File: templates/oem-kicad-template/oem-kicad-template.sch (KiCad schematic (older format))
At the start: 25 parts

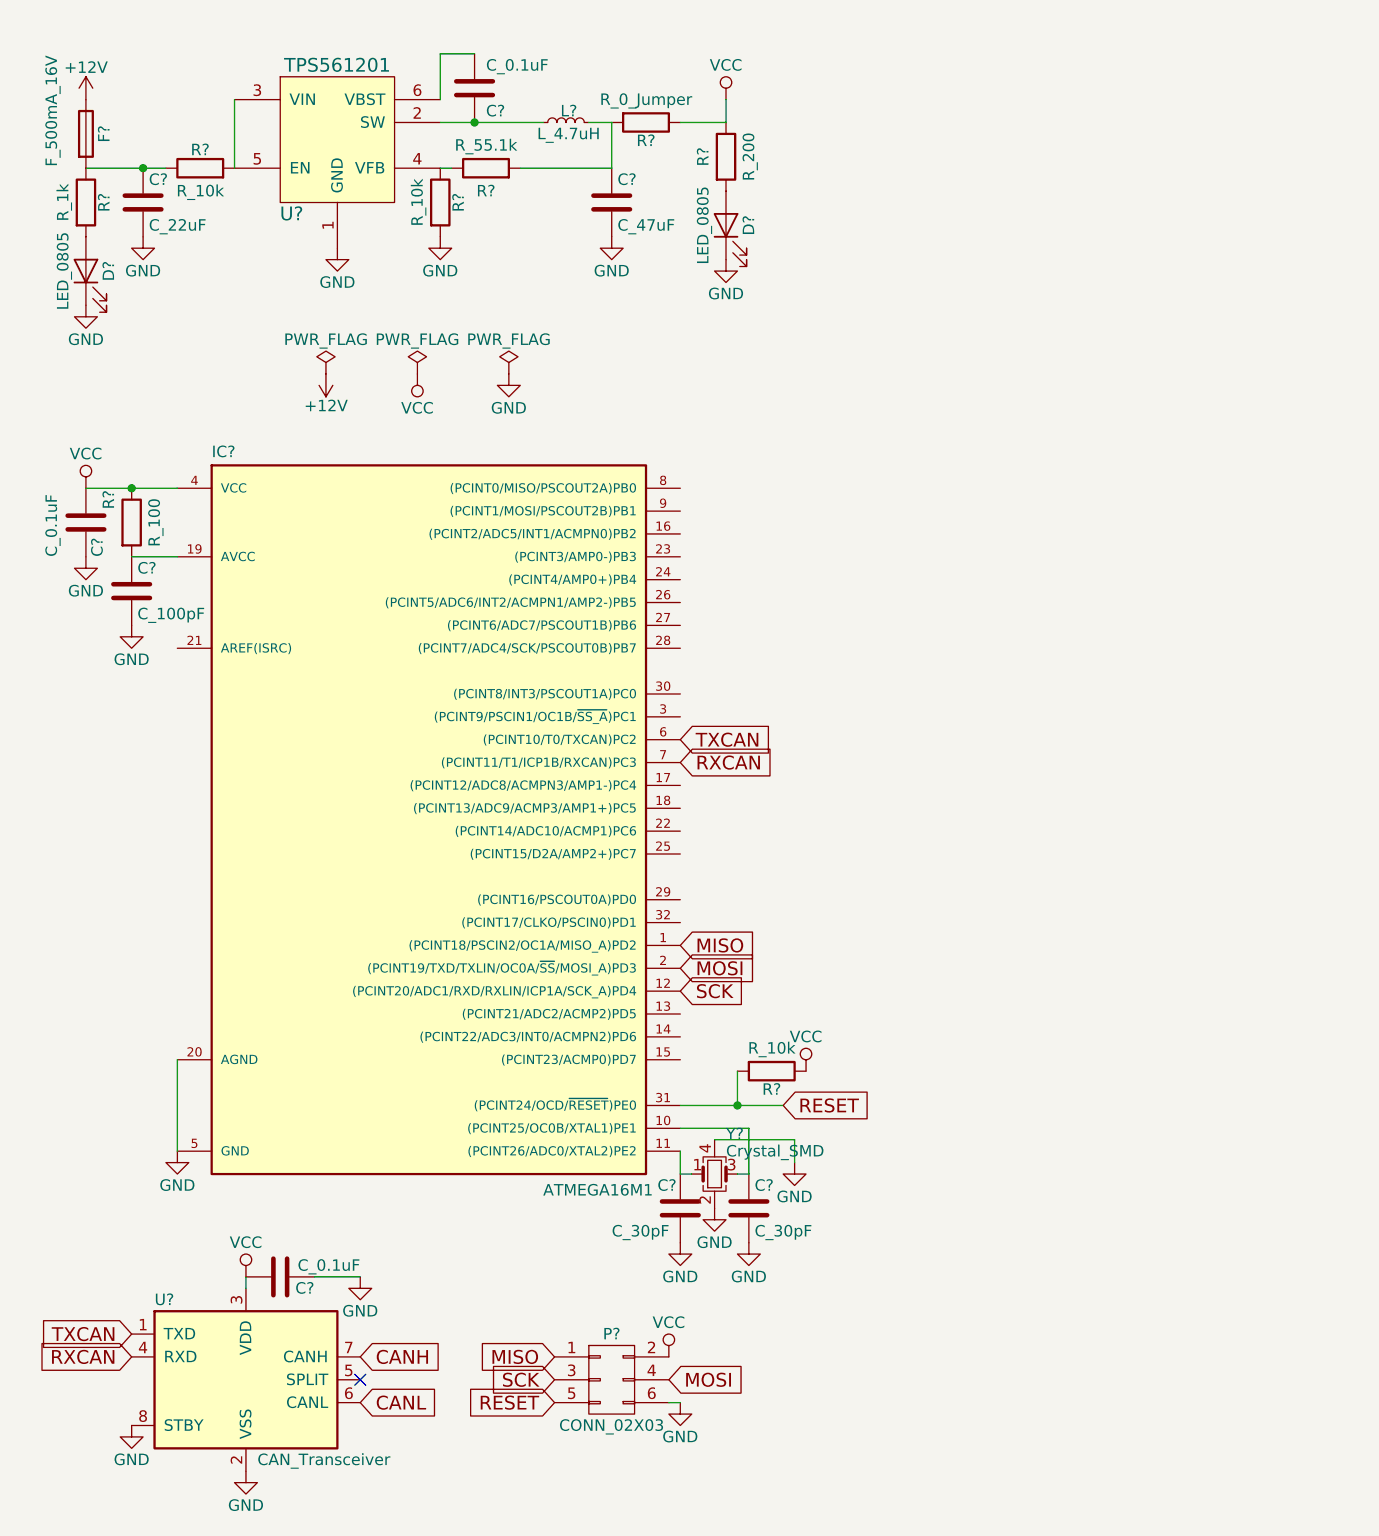
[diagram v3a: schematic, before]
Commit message: added some text to the reference schematic
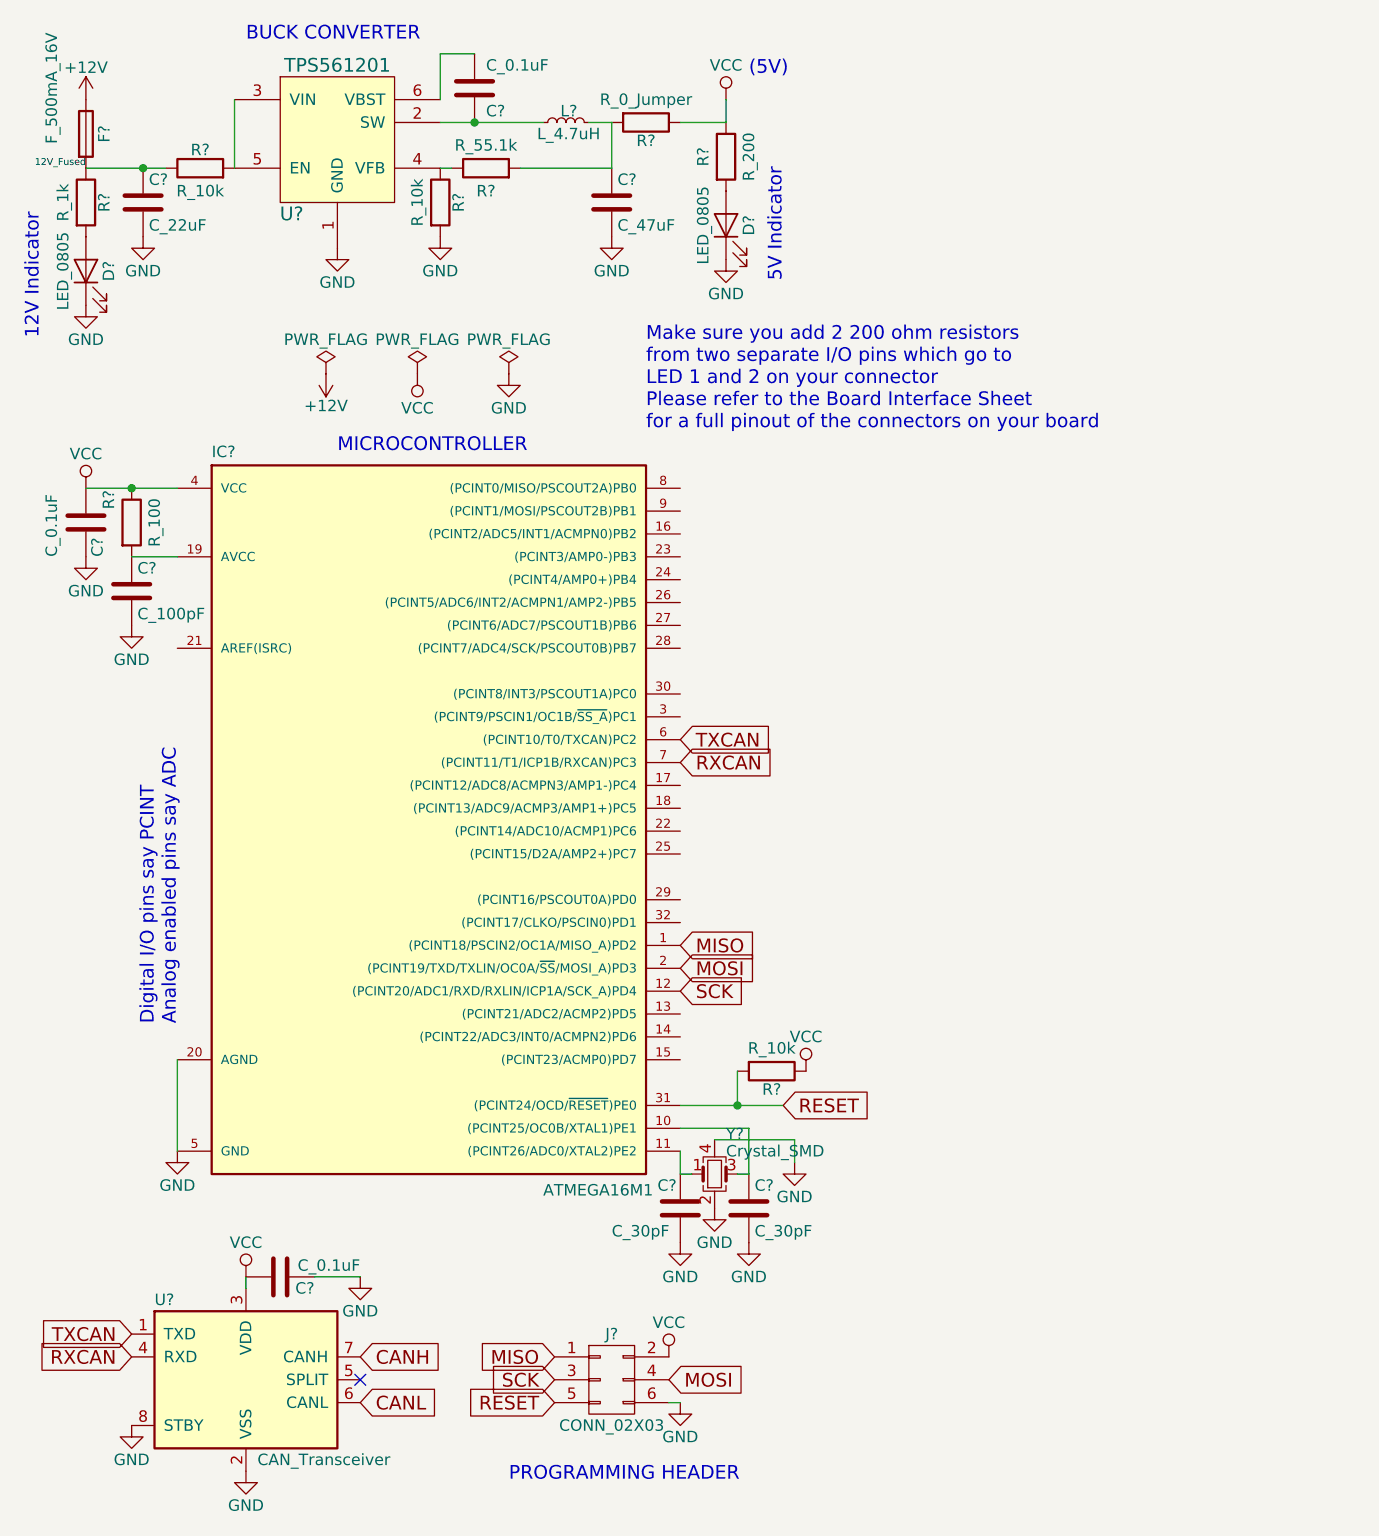
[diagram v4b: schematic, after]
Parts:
- gave numbers to parts that had none: 1
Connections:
- net 12V_Fused: now reaches C?.1, F?.2, R?.1, R?.1
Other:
- note added: "(5V)"
- note added: "12V Indicator"
- note added: "5V Indicator"
- note added: "BUCK CONVERTER"
- note added: "Digital I/O pins say PCINT\nAnalog enabled pins say ADC"
- note added: "MICROCONTROLLER"
- note added: "Make sure you add 2 200 ohm resistors\nfrom two separate I/O pins which go to\nLED 1 and 2 on your connector\nPlease refer to the Board Interface Sheet\nfor a full pinout of the connectors on your board"
- note added: "PROGRAMMING HEADER"
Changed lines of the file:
@@
 P 800 1000
 F 0 "F?" V 880 1000 50  0000 C CNN
-F 1 "F_500mA_16V" V 650 1100 50  0000 C CNN
+F 1 "F_500mA_16V" V 650 1200 50  0000 C CNN
 F 2 "footprints:Fuse_1210" V 730 1000 50  0001 C CNN
 F 3 "https://belfuse.com/resources/CircuitProtection/datasheets/0ZCH%20Nov2016.pdf" V 880 1000 50  0001 C CNN
@@
 	1450 850  1450 1150
 Wire Wire Line
-	2350 950  2800 950
+	2350 950  2500 950
+Wire Wire Line
+	2500 950  2800 950
 Wire Wire Line
 	2350 850  2350 650
@@
 $EndComp
 Wire Wire Line
-	800  2550 1200 2550
+	800  2550 1000 2550
+Wire Wire Line
+	1000 2550 1200 2550
 Connection ~ 1000 2550
 Wire Wire Line
-	800  1150 1150 1150
+	800  1150 1050 1150
+Wire Wire Line
+	1050 1150 1150 1150
 Connection ~ 1050 1150
 Wire Wire Line
-	3400 5250 3850 5250
+	3400 5250 3650 5250
+Wire Wire Line
+	3650 5250 3850 5250
 Wire Wire Line
 	3650 5100 3650 5250
@@
 $EndComp
 $Comp
-L CONN_02X03 P?
+L CONN_02X03 J?
 U 1 1 59E10F9E
 P 3100 6450
-F 0 "P?" H 3100 6650 50  0000 C CNN
+F 0 "J?" H 3100 6650 50  0000 C CNN
 F 1 "CONN_02X03" H 3100 6250 50  0000 C CNN
 F 2 "footprints:Pin_Header_Straight_2x03" H 3100 5250 50  0001 C CNN
 F 3 "http://portal.fciconnect.com/Comergent//fci/drawing/67996.pdf" H 3100 5250 50  0001 C CNN
-F 4 "609-3234-ND" H 3100 6450 60  0001 C CNN "MPN"
-F 5 "Digi-Key" H 3100 6450 60  0001 C CNN "MFN"
+F 4 "Digi-Key" H 3100 6450 60  0001 C CNN "MFN"
+F 5 "609-3234-ND" H 3100 6450 60  0001 C CNN "MPN"
 F 6 "Value" H 3100 6450 60  0001 C CNN "Package"
 F 7 "https://www.digikey.com/product-detail/en/amphenol-fci/67997-206HLF/609-3234-ND/1878491" H 3500 7050 60  0001 C CNN "PurchasingLink"
@@
 	1    0    0    -1
 $EndComp
+Text Notes 1500 600  0    60   ~ 0
+BUCK CONVERTER
+Text Label 800  1150 2    30   ~ 0
+12V_Fused
+Text Notes 600  1900 1    60   ~ 0
+12V Indicator
+Text Notes 3850 1650 1    60   ~ 0
+5V Indicator
+Text Notes 3700 750  0    60   ~ 0
+(5V)
+Text Notes 1900 2400 0    60   ~ 0
+MICROCONTROLLER
+Text Notes 2650 6900 0    60   ~ 0
+PROGRAMMING HEADER
+Text Notes 1200 4900 1    60   ~ 0
+Digital I/O pins say PCINT\nAnalog enabled pins say ADC
+Text Notes 3250 2300 0    60   ~ 0
+Make sure you add 2 200 ohm resistors\nfrom two separate I/O pins which go to\nLED 1 and 2 on your connector\nPlease refer to the Board Interface Sheet\nfor a full pinout of the connectors on your board
 $EndSCHEMATC

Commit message: added more text and changed to net labels
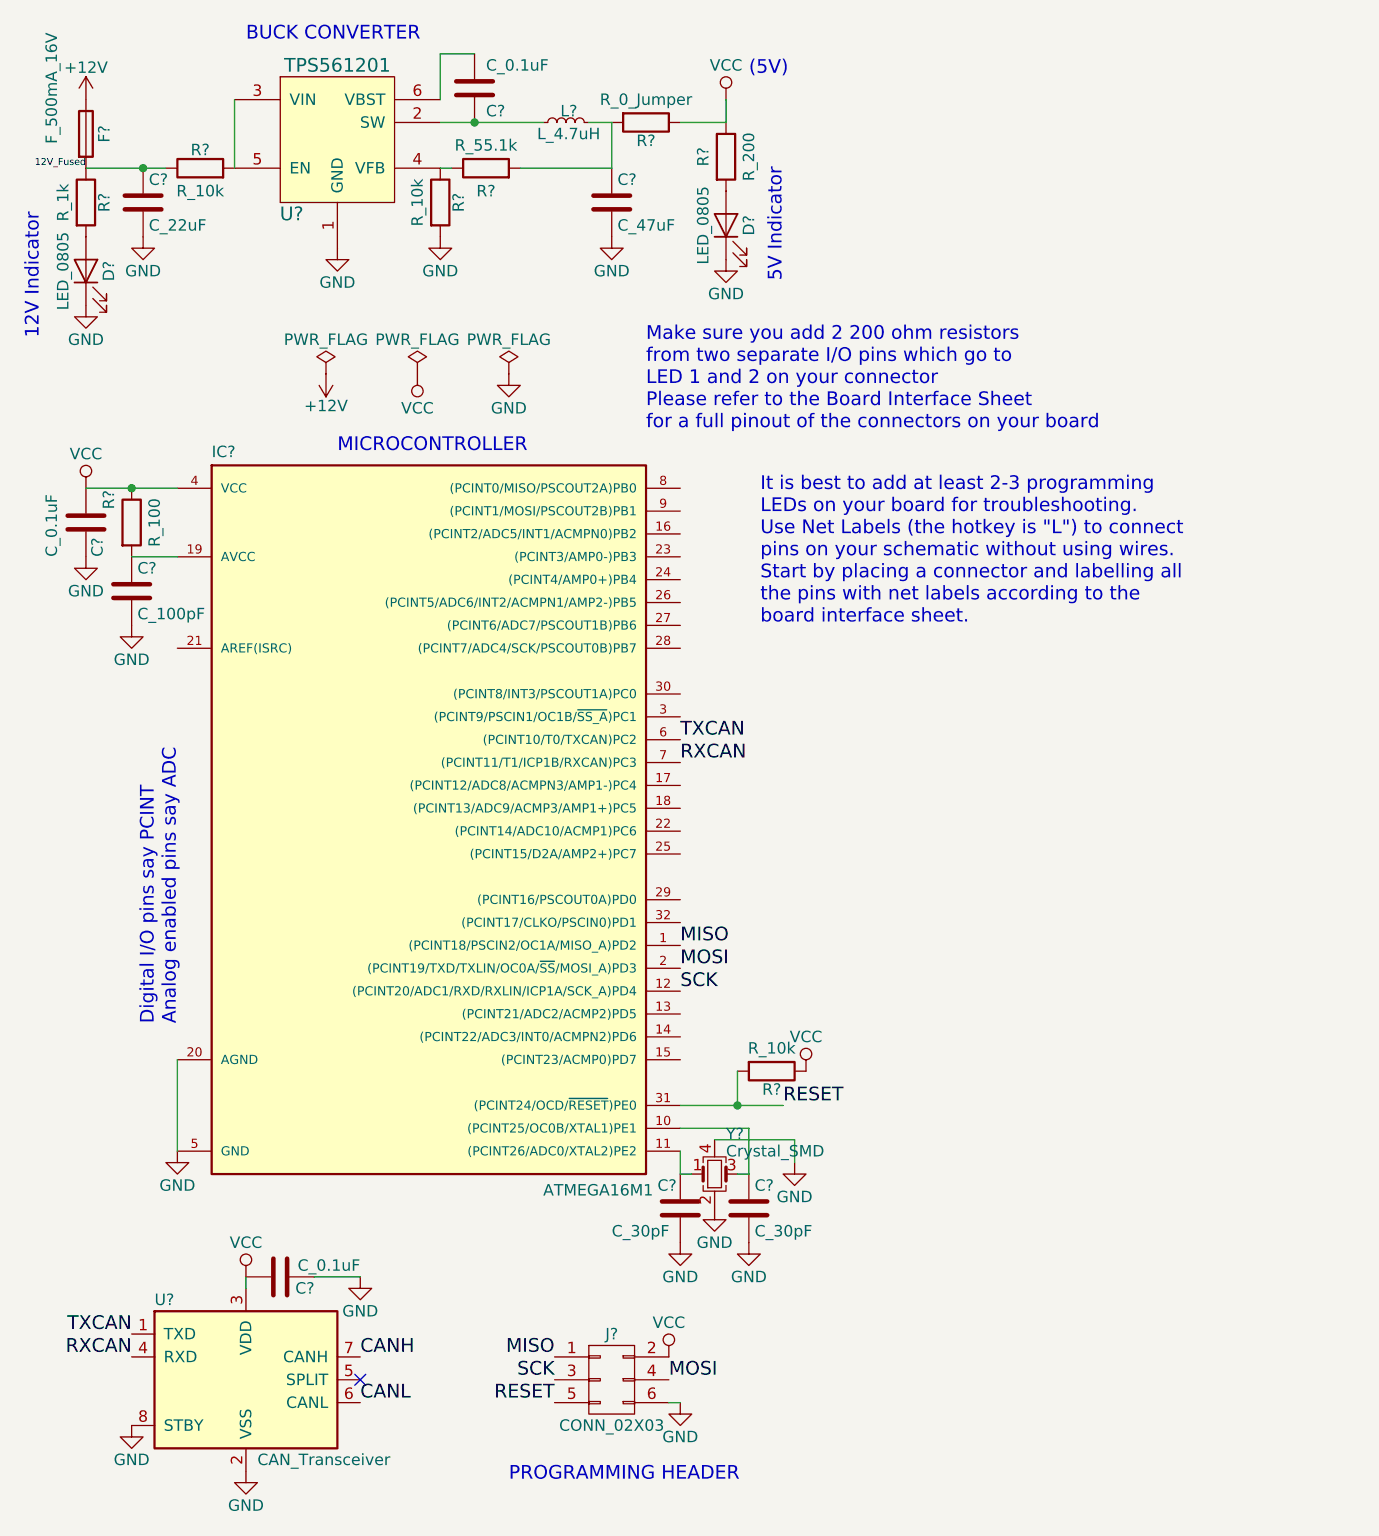
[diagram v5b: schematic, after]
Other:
- note added: "It is best to add at least 2-3 programming\nLEDs on your board for troubleshooting.\nUse Net Labels (the hotkey is "L") to connect\npins on your schematic without using wires.\nStart by placing a connector and labelling all\nthe pins with net labels according to the\nboard interface sheet."
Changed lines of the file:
@@
 	1    0    0    -1
 $EndComp
-Text GLabel 3850 5250 2    60   Input ~ 0
-RESET
 $Comp
 L VCC #PWR027
@@
 Wire Wire Line
 	3350 6550 3400 6550
-Text GLabel 3350 6450 2    60   Input ~ 0
-MOSI
-Text GLabel 2850 6350 0    60   Input ~ 0
-MISO
-Text GLabel 2850 6450 0    60   Input ~ 0
-SCK
-Text GLabel 2850 6550 0    60   Input ~ 0
-RESET
-Text GLabel 1000 6250 0    60   Input ~ 0
-TXCAN
-Text GLabel 1000 6350 0    60   Input ~ 0
-RXCAN
-Text GLabel 2000 6350 2    60   Input ~ 0
-CANH
-Text GLabel 2000 6550 2    60   Input ~ 0
-CANL
-Text GLabel 3400 4550 2    60   Input ~ 0
-MISO
-Text GLabel 3400 4650 2    60   Input ~ 0
-MOSI
-Text GLabel 3400 4750 2    60   Input ~ 0
-SCK
-Text GLabel 3400 3650 2    60   Input ~ 0
-TXCAN
-Text GLabel 3400 3750 2    60   Input ~ 0
-RXCAN
 $Comp
 L ATMEGA16M1 IC?
@@
 Text Notes 3250 2300 0    60   ~ 0
 Make sure you add 2 200 ohm resistors\nfrom two separate I/O pins which go to\nLED 1 and 2 on your connector\nPlease refer to the Board Interface Sheet\nfor a full pinout of the connectors on your board
+Text Label 2000 6550 0    60   ~ 0
+CANL
+Text Label 2000 6350 0    60   ~ 0
+CANH
+Text Label 1000 6250 2    60   ~ 0
+TXCAN
+Text Label 1000 6350 2    60   ~ 0
+RXCAN
+Text Label 3400 3650 0    60   ~ 0
+TXCAN
+Text Label 3400 3750 0    60   ~ 0
+RXCAN
+Text Label 3400 4550 0    60   ~ 0
+MISO
+Text Label 3400 4650 0    60   ~ 0
+MOSI
+Text Label 3400 4750 0    60   ~ 0
+SCK
+Text Label 3850 5250 0    60   ~ 0
+RESET
+Text Label 2850 6350 2    60   ~ 0
+MISO
+Text Label 2850 6450 2    60   ~ 0
+SCK
+Text Label 2850 6550 2    60   ~ 0
+RESET
+Text Label 3350 6450 0    60   ~ 0
+MOSI
+Text Notes 3750 3150 0    60   ~ 0
+It is best to add at least 2-3 programming\nLEDs on your board for troubleshooting.\nUse Net Labels (the hotkey is "L") to connect\npins on your schematic without using wires.\nStart by placing a connector and labelling all\nthe pins with net labels according to the\nboard interface sheet.
 $EndSCHEMATC

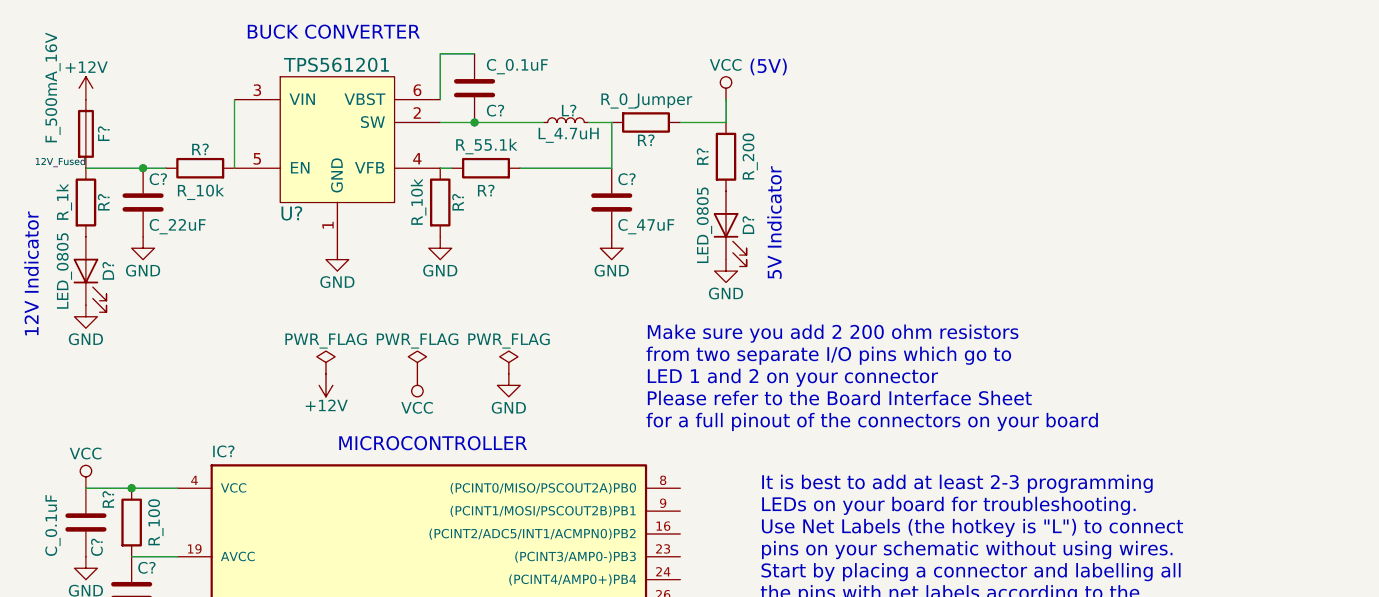
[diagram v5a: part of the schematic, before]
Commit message: edited discharge circuit schematic
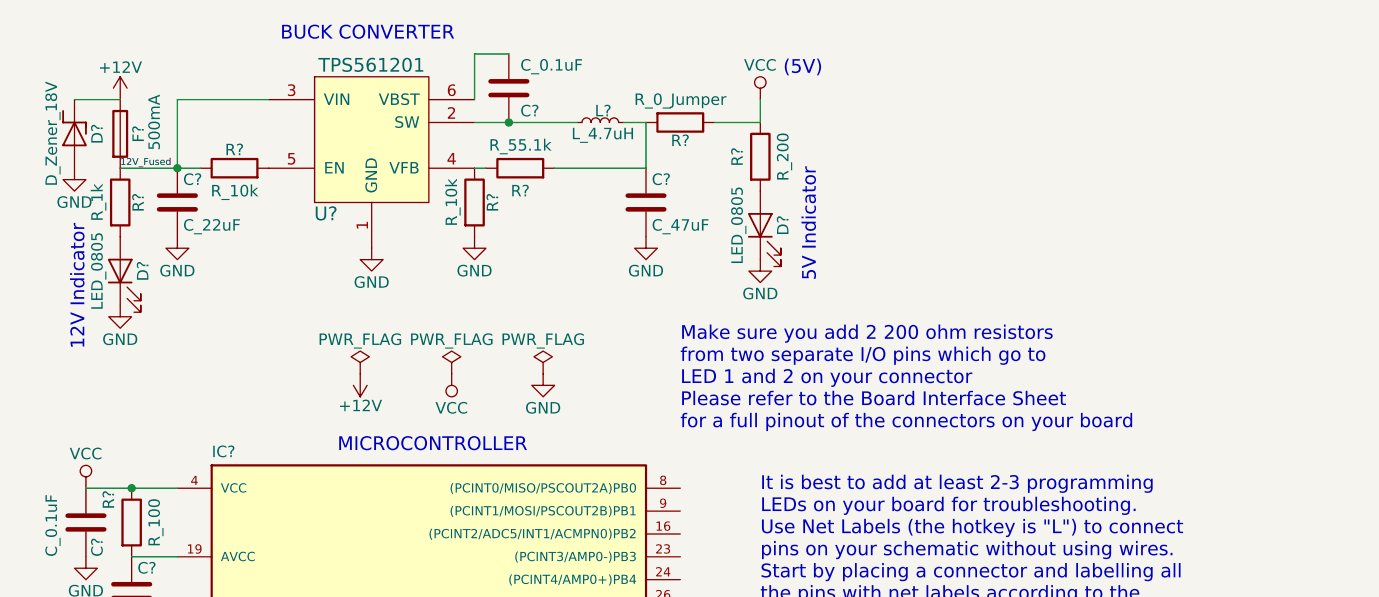
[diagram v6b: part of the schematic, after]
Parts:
- added D?: D_Zener_18V, footprints:DO-214AA, symbol D_Zener_18V
- F?: value F_500mA_16V -> 500mA
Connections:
- net +12V: now also D?.1 (K)
- net 12V_Fused: now also U?.3 (VIN)
- net GND: now also D?.2 (A)
- net at R?.2, U?.5 (EN): no longer U?.3 (VIN)
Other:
- moved on the sheet: C?, D?, F?, L?, R?, U?
